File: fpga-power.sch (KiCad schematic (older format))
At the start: 17 parts

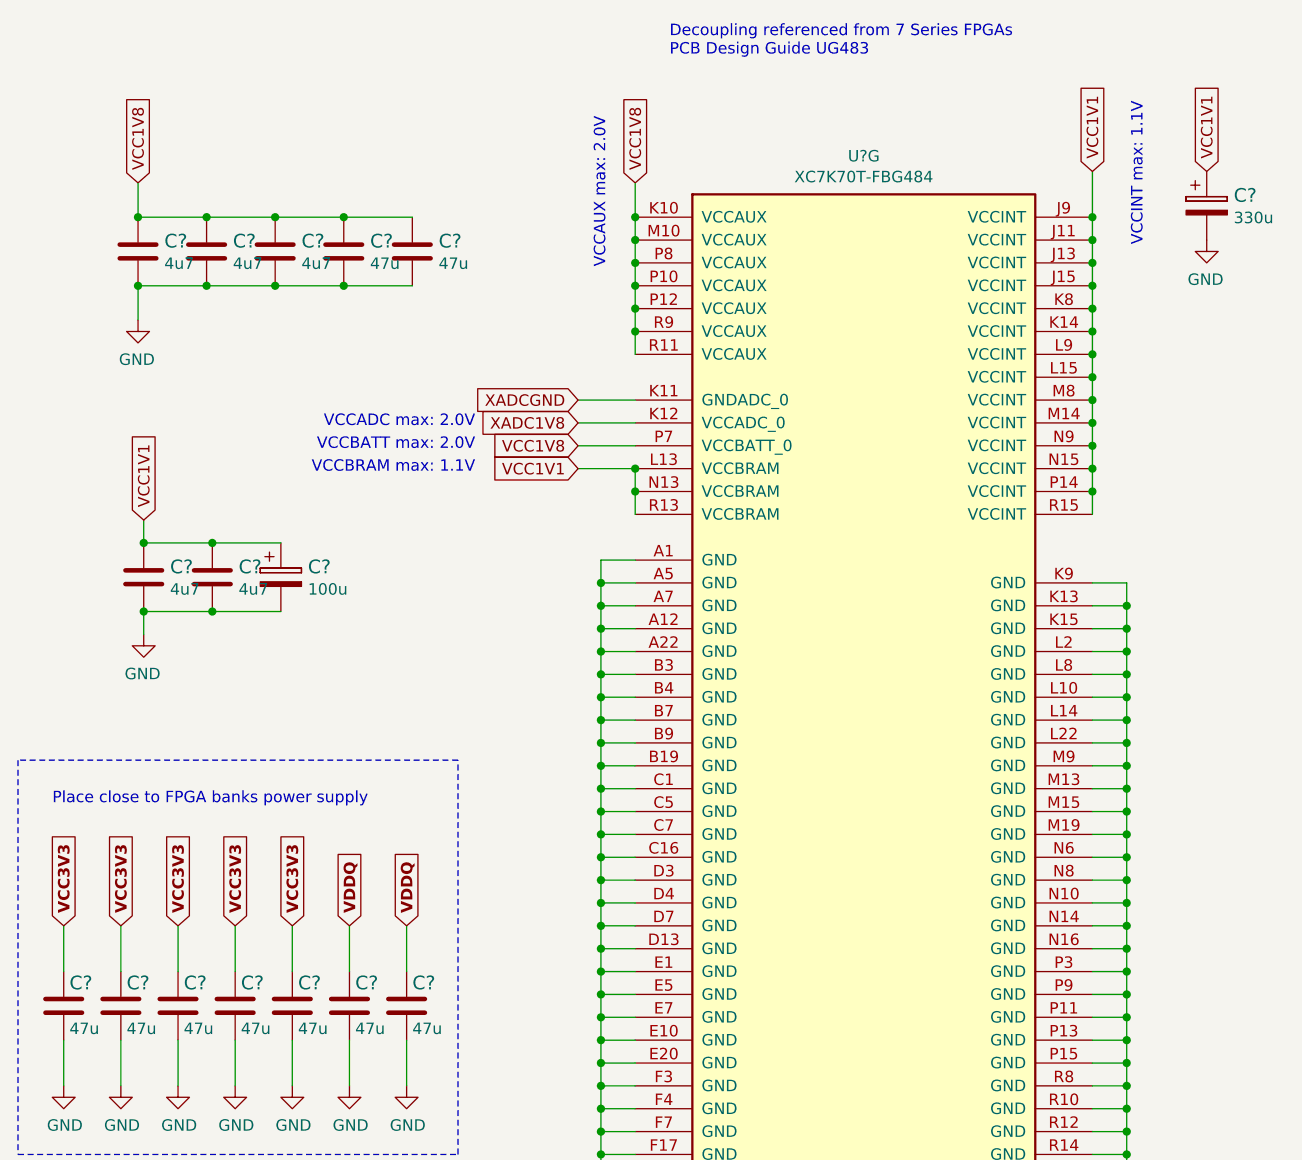
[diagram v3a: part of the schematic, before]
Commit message: Library cleanup, add RGMII layout
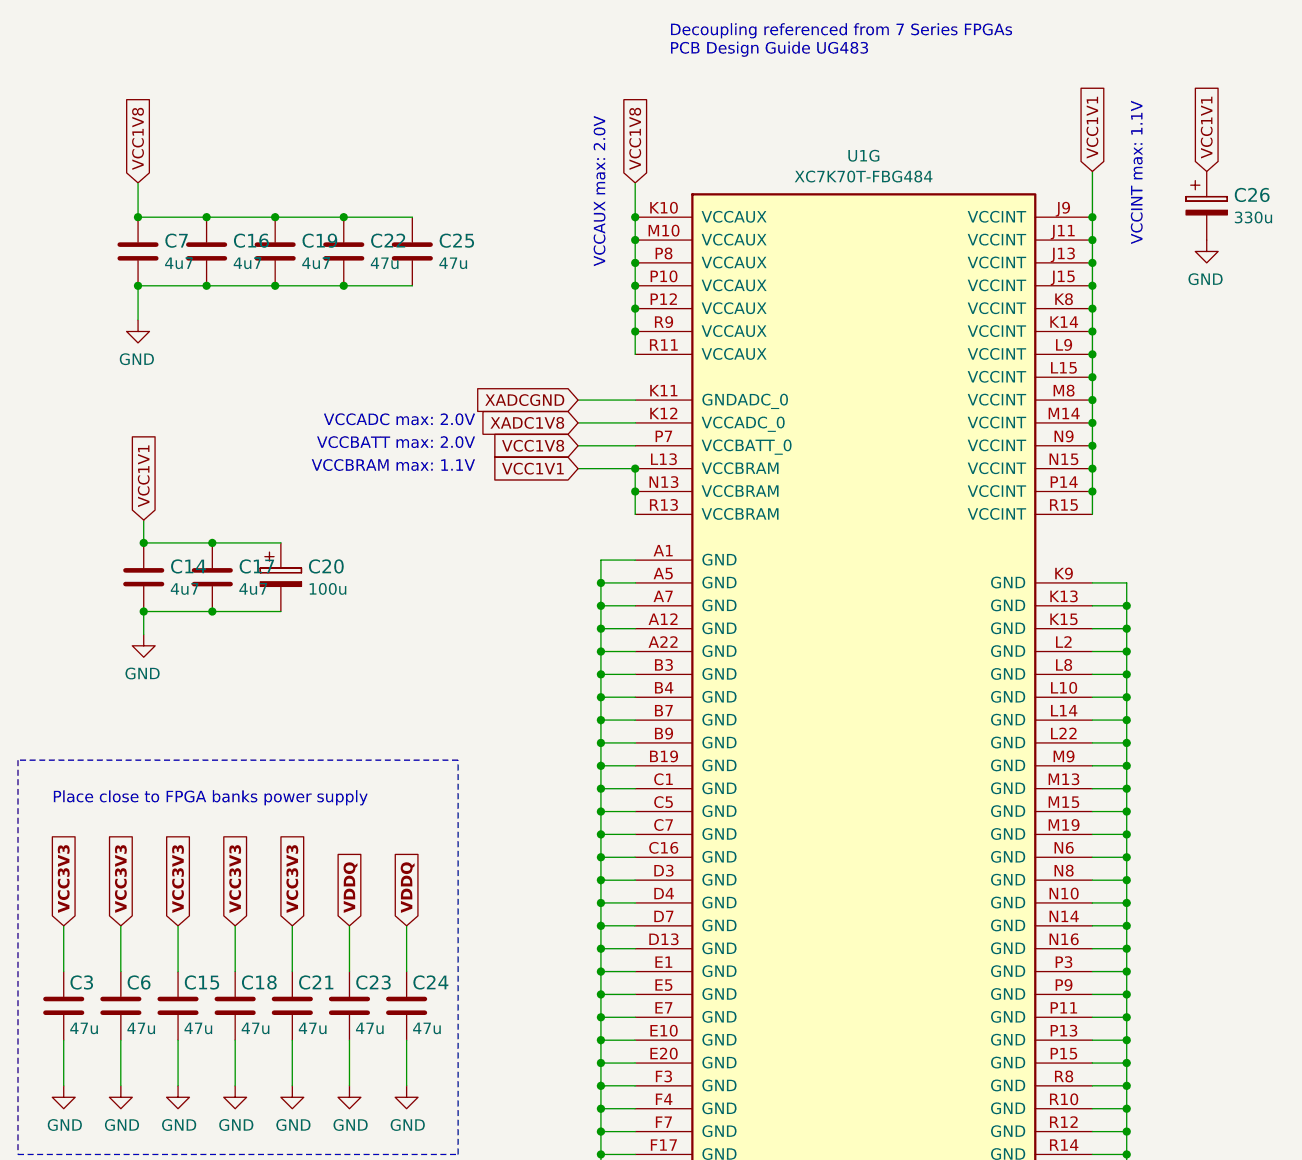
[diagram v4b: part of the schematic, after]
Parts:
- gave numbers to parts that had none: 17
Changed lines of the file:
@@
 VCC1V8
 $Comp
-L lpddr4-test-board:XC7K70T-FBG484 U?
+L lpddr4-test-board:XC7K70T-FBG484 U1
 U 7 1 6246CC56
 P 8525 5325
-F 0 "U?" H 8525 8492 50  0000 C CNN
+F 0 "U1" H 8525 8492 50  0000 C CNN
 F 1 "XC7K70T-FBG484" H 8525 8401 50  0000 C CNN
 F 2 "lpddr4-test-board-footprints:BGA484C100P22X22_2300X2300X244N" H 8525 5325 50  0001 C CNN
@@
 	9675 5425 9675 5525
 $Comp
-L lpddr4-test-board:GND #PWR?
+L lpddr4-test-board:GND #PWR0121
 U 1 1 6259B1A2
 P 9675 8825
-F 0 "#PWR?" H 9675 8575 50  0001 C CNN
+F 0 "#PWR0121" H 9675 8575 50  0001 C CNN
 F 1 "GND" H 9680 8652 50  0000 C CNN
 F 2 "" H 9675 8825 50  0001 C CNN
@@
 Connection ~ 7525 2425
 $Comp
-L lpddr4-test-board:C_47u_0603 C?
+L lpddr4-test-board:C_47u_0603 C22
 U 1 1 64DC1502
 P 6250 2575
-F 0 "C?" H 6365 2620 60  0000 L CNN
+F 0 "C22" H 6365 2620 60  0000 L CNN
 F 1 "C_47u_0603" H 6250 2425 60  0001 C CNN
 F 2 "lpddr4-test-board-footprints:0603-cap" H 6450 2775 60  0001 L CNN
@@
 $EndComp
 $Comp
-L lpddr4-test-board:C_47u_0603 C?
+L lpddr4-test-board:C_47u_0603 C25
 U 1 1 64DC1D53
 P 6550 2575
-F 0 "C?" H 6665 2620 60  0000 L CNN
+F 0 "C25" H 6665 2620 60  0000 L CNN
 F 1 "C_47u_0603" H 6550 2425 60  0001 C CNN
 F 2 "lpddr4-test-board-footprints:0603-cap" H 6750 2775 60  0001 L CNN
@@
 $EndComp
 $Comp
-L lpddr4-test-board:C_4u7_0402 C?
+L lpddr4-test-board:C_4u7_0402 C19
 U 1 1 64DC2DD0
 P 5950 2575
-F 0 "C?" H 6065 2620 60  0000 L CNN
+F 0 "C19" H 6065 2620 60  0000 L CNN
 F 1 "C_4u7_0402" H 5950 2425 60  0001 C CNN
 F 2 "lpddr4-test-board-footprints:0402-cap" H 6150 2775 60  0001 L CNN
@@
 $EndComp
 $Comp
-L lpddr4-test-board:C_4u7_0402 C?
+L lpddr4-test-board:C_4u7_0402 C16
 U 1 1 64DC3787
 P 5650 2575
-F 0 "C?" H 5765 2620 60  0000 L CNN
+F 0 "C16" H 5765 2620 60  0000 L CNN
 F 1 "C_4u7_0402" H 5650 2425 60  0001 C CNN
 F 2 "lpddr4-test-board-footprints:0402-cap" H 5850 2775 60  0001 L CNN
@@
 $EndComp
 $Comp
-L lpddr4-test-board:C_4u7_0402 C?
+L lpddr4-test-board:C_4u7_0402 C7
 U 1 1 64DC3EBA
 P 5350 2575
-F 0 "C?" H 5465 2620 60  0000 L CNN
+F 0 "C7" H 5465 2620 60  0000 L CNN
 F 1 "C_4u7_0402" H 5350 2425 60  0001 C CNN
 F 2 "lpddr4-test-board-footprints:0402-cap" H 5550 2775 60  0001 L CNN
@@
 	6250 2725 5950 2725
 $Comp
-L lpddr4-test-board:GND #PWR?
+L lpddr4-test-board:GND #PWR0122
 U 1 1 64FA6D96
 P 5350 2875
-F 0 "#PWR?" H 5350 2625 50  0001 C CNN
+F 0 "#PWR0122" H 5350 2625 50  0001 C CNN
 F 1 "GND" H 5355 2702 50  0000 C CNN
 F 2 "" H 5350 2875 50  0001 C CNN
@@
 	7275 3525 7525 3525
 $Comp
-L lpddr4-test-board:C_100u_KEMET_A C?
+L lpddr4-test-board:C_100u_KEMET_A C20
 U 1 1 6517E142
 P 5975 3950
-F 0 "C?" H 6093 3945 60  0000 L CNN
+F 0 "C20" H 6093 3945 60  0000 L CNN
 F 1 "C_100u_KEMET_A" H 5975 3800 60  0001 C CNN
 F 2 "lpddr4-test-board-footprints:KEMET_A" H 6175 4150 60  0001 L CNN
@@
 $EndComp
 $Comp
-L lpddr4-test-board:C_4u7_0402 C?
+L lpddr4-test-board:C_4u7_0402 C17
 U 1 1 65180351
 P 5675 4000
-F 0 "C?" H 5790 4045 60  0000 L CNN
+F 0 "C17" H 5790 4045 60  0000 L CNN
 F 1 "C_4u7_0402" H 5675 3850 60  0001 C CNN
 F 2 "lpddr4-test-board-footprints:0402-cap" H 5875 4200 60  0001 L CNN
@@
 $EndComp
 $Comp
-L lpddr4-test-board:C_4u7_0402 C?
+L lpddr4-test-board:C_4u7_0402 C14
 U 1 1 6518A43F
 P 5375 4000
-F 0 "C?" H 5490 4045 60  0000 L CNN
+F 0 "C14" H 5490 4045 60  0000 L CNN
 F 1 "C_4u7_0402" H 5375 3850 60  0001 C CNN
 F 2 "lpddr4-test-board-footprints:0402-cap" H 5575 4200 60  0001 L CNN
@@
 	5675 4150 5375 4150
 $Comp
-L lpddr4-test-board:GND #PWR?
+L lpddr4-test-board:GND #PWR0123
 U 1 1 6527545F
 P 5375 4250
-F 0 "#PWR?" H 5375 4000 50  0001 C CNN
+F 0 "#PWR0123" H 5375 4000 50  0001 C CNN
 F 1 "GND" H 5380 4077 50  0000 C CNN
 F 2 "" H 5375 4250 50  0001 C CNN
@@
 $EndComp
 $Comp
-L lpddr4-test-board:C_330u_KEMET_D C?
+L lpddr4-test-board:C_330u_KEMET_D C26
 U 1 1 653DADFB
 P 10025 2325
-F 0 "C?" H 10143 2320 60  0000 L CNN
+F 0 "C26" H 10143 2320 60  0000 L CNN
 F 1 "C_330u_KEMET_D" H 10025 2175 60  0001 C CNN
 F 2 "lpddr4-test-board-footprints:KEMET_D" H 10225 2525 60  0001 L CNN
@@
 	9525 2425 9525 2525
 $Comp
-L lpddr4-test-board:GND #PWR?
+L lpddr4-test-board:GND #PWR0124
 U 1 1 6545DAEF
 P 10025 2525
-F 0 "#PWR?" H 10025 2275 50  0001 C CNN
+F 0 "#PWR0124" H 10025 2275 50  0001 C CNN
 F 1 "GND" H 10030 2352 50  0000 C CNN
 F 2 "" H 10025 2525 50  0001 C CNN
@@
 P 5025 5875
 AR Path="/5F96C515/60613726" Ref="C?"  Part="1"
-AR Path="/600295C1/60613726" Ref="C?"  Part="1"
-F 0 "C?" H 5050 5975 60  0000 L CNN
+AR Path="/600295C1/60613726" Ref="C3"  Part="1"
+F 0 "C3" H 5050 5975 60  0000 L CNN
 F 1 "C_47u_0603" H 5025 5725 60  0001 C CNN
 F 2 "lpddr4-test-board-footprints:0603-cap" H 5225 6075 60  0001 L CNN
@@
 P 5275 5875
 AR Path="/5F96C515/6061372F" Ref="C?"  Part="1"
-AR Path="/600295C1/6061372F" Ref="C?"  Part="1"
-F 0 "C?" H 5300 5975 60  0000 L CNN
+AR Path="/600295C1/6061372F" Ref="C6"  Part="1"
+F 0 "C6" H 5300 5975 60  0000 L CNN
 F 1 "C_47u_0603" H 5275 5725 60  0001 C CNN
 F 2 "lpddr4-test-board-footprints:0603-cap" H 5475 6075 60  0001 L CNN
@@
 P 5525 5875
 AR Path="/5F96C515/60613738" Ref="C?"  Part="1"
-AR Path="/600295C1/60613738" Ref="C?"  Part="1"
-F 0 "C?" H 5550 5975 60  0000 L CNN
+AR Path="/600295C1/60613738" Ref="C15"  Part="1"
+F 0 "C15" H 5550 5975 60  0000 L CNN
 F 1 "C_47u_0603" H 5525 5725 60  0001 C CNN
 F 2 "lpddr4-test-board-footprints:0603-cap" H 5725 6075 60  0001 L CNN
@@
 P 5775 5875
 AR Path="/5F96C515/60613741" Ref="C?"  Part="1"
-AR Path="/600295C1/60613741" Ref="C?"  Part="1"
-F 0 "C?" H 5800 5975 60  0000 L CNN
+AR Path="/600295C1/60613741" Ref="C18"  Part="1"
+F 0 "C18" H 5800 5975 60  0000 L CNN
 F 1 "C_47u_0603" H 5775 5725 60  0001 C CNN
 F 2 "lpddr4-test-board-footprints:0603-cap" H 5975 6075 60  0001 L CNN
@@
 P 6025 5875
 AR Path="/5F96C515/6061374A" Ref="C?"  Part="1"
-AR Path="/600295C1/6061374A" Ref="C?"  Part="1"
-F 0 "C?" H 6050 5975 60  0000 L CNN
+AR Path="/600295C1/6061374A" Ref="C21"  Part="1"
+F 0 "C21" H 6050 5975 60  0000 L CNN
 F 1 "C_47u_0603" H 6025 5725 60  0001 C CNN
 F 2 "lpddr4-test-board-footprints:0603-cap" H 6225 6075 60  0001 L CNN
@@
 P 6275 5875
 AR Path="/5F96C515/60613753" Ref="C?"  Part="1"
-AR Path="/600295C1/60613753" Ref="C?"  Part="1"
-F 0 "C?" H 6300 5975 60  0000 L CNN
+AR Path="/600295C1/60613753" Ref="C23"  Part="1"
+F 0 "C23" H 6300 5975 60  0000 L CNN
 F 1 "C_47u_0603" H 6275 5725 60  0001 C CNN
 F 2 "lpddr4-test-board-footprints:0603-cap" H 6475 6075 60  0001 L CNN
@@
 P 6525 5875
 AR Path="/5F96C515/6061375C" Ref="C?"  Part="1"
-AR Path="/600295C1/6061375C" Ref="C?"  Part="1"
-F 0 "C?" H 6550 5975 60  0000 L CNN
+AR Path="/600295C1/6061375C" Ref="C24"  Part="1"
+F 0 "C24" H 6550 5975 60  0000 L CNN
 F 1 "C_47u_0603" H 6525 5725 60  0001 C CNN
 F 2 "lpddr4-test-board-footprints:0603-cap" H 6725 6075 60  0001 L CNN
@@
 P 5025 6225
 AR Path="/5F96C515/60613770" Ref="#PWR?"  Part="1"
-AR Path="/600295C1/60613770" Ref="#PWR?"  Part="1"
-F 0 "#PWR?" H 5025 5975 50  0001 C CNN
+AR Path="/600295C1/60613770" Ref="#PWR0125"  Part="1"
+F 0 "#PWR0125" H 5025 5975 50  0001 C CNN
 F 1 "GND" H 5030 6052 50  0000 C CNN
 F 2 "" H 5025 6225 50  0001 C CNN
@@
 P 5275 6225
 AR Path="/5F96C515/60613776" Ref="#PWR?"  Part="1"
-AR Path="/600295C1/60613776" Ref="#PWR?"  Part="1"
-F 0 "#PWR?" H 5275 5975 50  0001 C CNN
+AR Path="/600295C1/60613776" Ref="#PWR0126"  Part="1"
+F 0 "#PWR0126" H 5275 5975 50  0001 C CNN
 F 1 "GND" H 5280 6052 50  0000 C CNN
 F 2 "" H 5275 6225 50  0001 C CNN
@@
 P 5525 6225
 AR Path="/5F96C515/6061377C" Ref="#PWR?"  Part="1"
-AR Path="/600295C1/6061377C" Ref="#PWR?"  Part="1"
-F 0 "#PWR?" H 5525 5975 50  0001 C CNN
+AR Path="/600295C1/6061377C" Ref="#PWR0127"  Part="1"
+F 0 "#PWR0127" H 5525 5975 50  0001 C CNN
 F 1 "GND" H 5530 6052 50  0000 C CNN
 F 2 "" H 5525 6225 50  0001 C CNN
@@
 P 5775 6225
 AR Path="/5F96C515/60613782" Ref="#PWR?"  Part="1"
-AR Path="/600295C1/60613782" Ref="#PWR?"  Part="1"
-F 0 "#PWR?" H 5775 5975 50  0001 C CNN
+AR Path="/600295C1/60613782" Ref="#PWR0128"  Part="1"
+F 0 "#PWR0128" H 5775 5975 50  0001 C CNN
 F 1 "GND" H 5780 6052 50  0000 C CNN
 F 2 "" H 5775 6225 50  0001 C CNN
@@
 P 6025 6225
 AR Path="/5F96C515/60613788" Ref="#PWR?"  Part="1"
-AR Path="/600295C1/60613788" Ref="#PWR?"  Part="1"
-F 0 "#PWR?" H 6025 5975 50  0001 C CNN
+AR Path="/600295C1/60613788" Ref="#PWR0129"  Part="1"
+F 0 "#PWR0129" H 6025 5975 50  0001 C CNN
 F 1 "GND" H 6030 6052 50  0000 C CNN
 F 2 "" H 6025 6225 50  0001 C CNN
@@
 P 6275 6225
 AR Path="/5F96C515/6061378E" Ref="#PWR?"  Part="1"
-AR Path="/600295C1/6061378E" Ref="#PWR?"  Part="1"
-F 0 "#PWR?" H 6275 5975 50  0001 C CNN
+AR Path="/600295C1/6061378E" Ref="#PWR0130"  Part="1"
+F 0 "#PWR0130" H 6275 5975 50  0001 C CNN
 F 1 "GND" H 6280 6052 50  0000 C CNN
 F 2 "" H 6275 6225 50  0001 C CNN
@@
 P 6525 6225
 AR Path="/5F96C515/60613794" Ref="#PWR?"  Part="1"
-AR Path="/600295C1/60613794" Ref="#PWR?"  Part="1"
-F 0 "#PWR?" H 6525 5975 50  0001 C CNN
+AR Path="/600295C1/60613794" Ref="#PWR0131"  Part="1"
+F 0 "#PWR0131" H 6525 5975 50  0001 C CNN
 F 1 "GND" H 6530 6052 50  0000 C CNN
 F 2 "" H 6525 6225 50  0001 C CNN

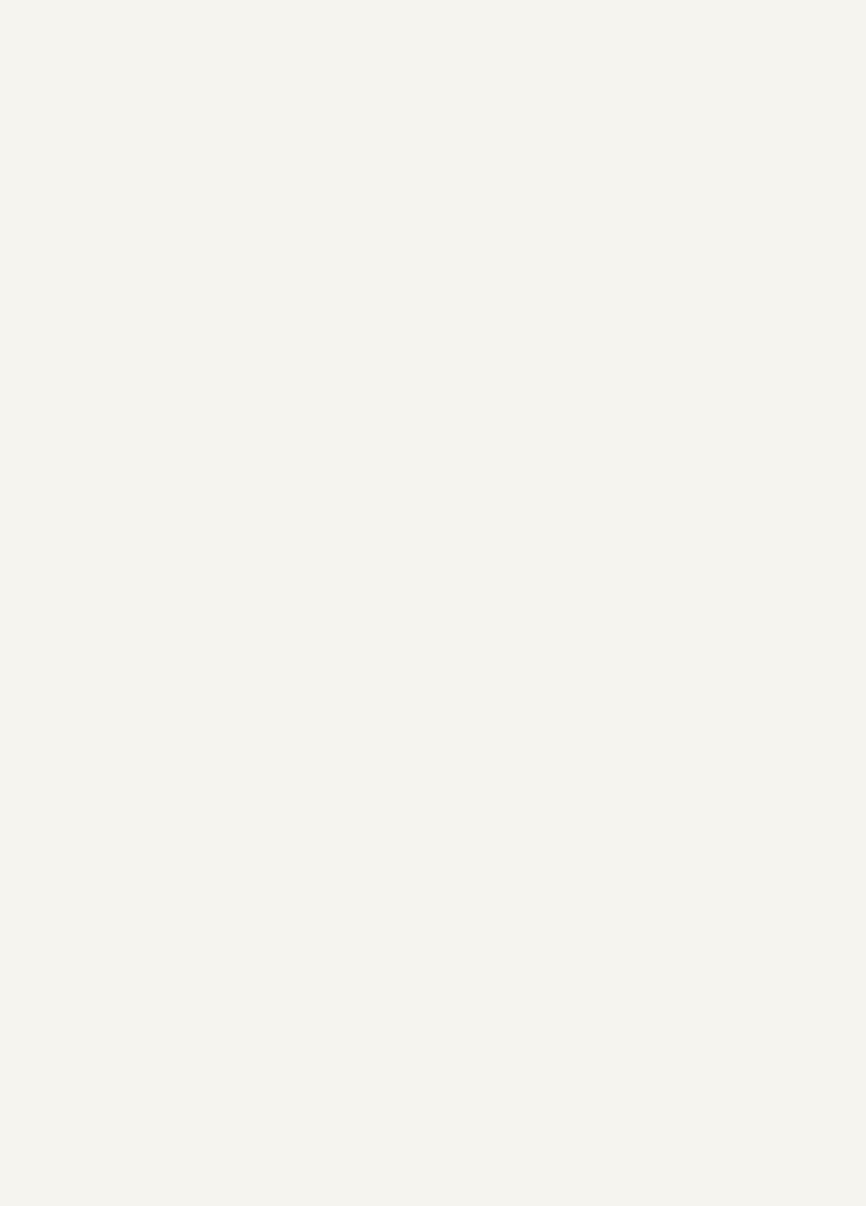
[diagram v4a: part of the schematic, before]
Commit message: Instantiate unused FPGA blocks
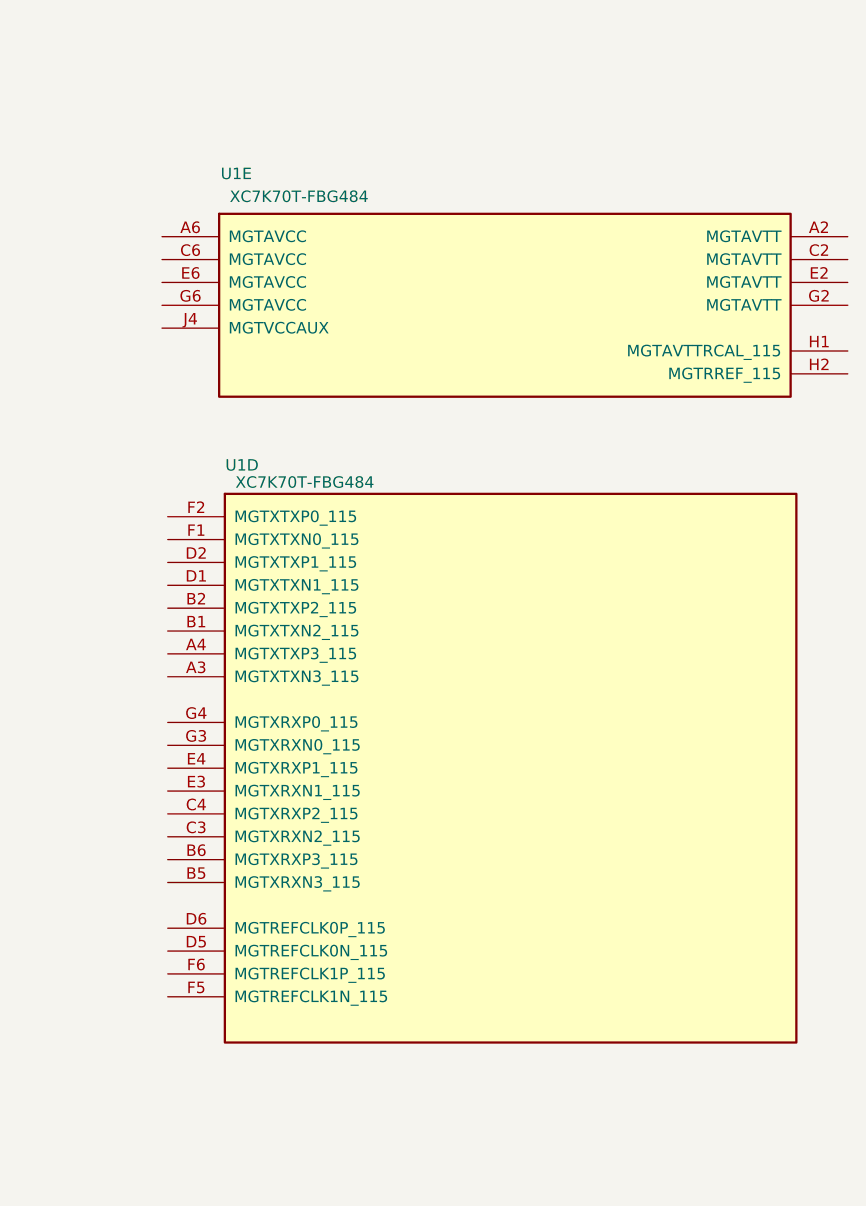
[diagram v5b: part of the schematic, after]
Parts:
- added unit 5 of U1
- added unit 4 of U1
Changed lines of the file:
@@
 Text GLabel 5375 3750 1    50   Input ~ 0
 VCC1V1
+$Comp
+L lpddr4-test-board:XC7K70T-FBG484 U1
+U 5 1 604C456D
+P 12975 4675
+F 0 "U1" H 11800 5250 50  0000 C CNN
+F 1 "XC7K70T-FBG484" H 12075 5150 50  0000 C CNN
+F 2 "lpddr4-test-board-footprints:BGA484C100P22X22_2300X2300X244N" H 12975 4675 50  0001 C CNN
+F 3 "" H 12975 4675 50  0000 C CNN
+	5    12975 4675
+	1    0    0    -1
+$EndComp
+$Comp
+L lpddr4-test-board:XC7K70T-FBG484 U1
+U 4 1 604D7DF0
+P 13000 6700
+F 0 "U1" H 11825 8025 50  0000 C CNN
+F 1 "XC7K70T-FBG484" H 12100 7950 50  0000 C CNN
+F 2 "lpddr4-test-board-footprints:BGA484C100P22X22_2300X2300X244N" H 13000 6700 50  0001 C CNN
+F 3 "" H 13000 6700 50  0000 C CNN
+	4    13000 6700
+	1    0    0    -1
+$EndComp
 $EndSCHEMATC
